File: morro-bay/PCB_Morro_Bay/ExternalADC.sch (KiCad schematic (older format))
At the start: 85 parts, among them SW4 SW_DIP_x12, U10 LM2902, U11 LM2902, U12 LM2902, U14 LM2902, U15 LM2902, U16 LM2902, U17 LM2902, U18 LM2902, U19 LM2902, U20 LM2902, U21 LM2902, U22 LM2902, U23 LM2902, U24 LM2902, U25 LM2902, U26 ADS114S08BIPBSR

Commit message: Even more BOM and footprints
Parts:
- removed C32, C66, C67, C68, C69: 0.1uF, Capacitor_SMD:C_0603_1608Metric_Pad1.05x0.95mm_HandSolder, symbol Device:C
- removed D31, D32, D33, D34: 3.3V, Diode_SMD:D_SOD-323_HandSoldering, symbol Device:D_Zener
- removed R101, R103, R105, R99: 100K, symbol Device:R_US
- removed R106, R107, R108, R109: 500, symbol Device:R_US
- removed U12, U22, U23, U24, U25: LM2902, symbol Amplifier_Operational:LM2902
- added U22: AD620, Package_SO:SOIC-8_3.9x4.9mm_P1.27mm, symbol Amplifier_Instrumentation:AD620
- R74, R76, R78, R80: footprint (none) -> Resistor_SMD:R_0603_1608Metric_Pad1.05x0.95mm_HandSolder; Digikey (none) -> https://www.digikey.ca/product-detail/en/panasonic-electron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; Part Number (none) -> ERJ-PB3B5112V
- R75, R77, R79, R81, R87, R89, R91, R93: footprint (none) -> Resistor_SMD:R_0603_1608Metric_Pad1.05x0.95mm_HandSolder; Digikey (none) -> https://www.digikey.ca/product-detail/en/panasonic-electron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; Part Number (none) -> ERJ-PB3B1003V
- R82, R83, R84, R85, R94, R95, R96, R97: value 500 -> 470; footprint (none) -> Resistor_SMD:R_0603_1608Metric_Pad1.05x0.95mm_HandSolder; Digikey (none) -> https://www.digikey.ca/product-detail/en/stackpole-electron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; Part Number (none) -> RMCF0603FT470R
- R86, R88, R90, R92: footprint (none) -> Resistor_SMD:R_0603_1608Metric_Pad1.05x0.95mm_HandSolder; Digikey (none) -> https://www.digikey.ca/product-detail/en/panasonic-electron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; Part Number (none) -> ERA-3AEB2053V
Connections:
- net 5V_IN_13 is gone; now on net 5V_IN_15: R74.1
- net 5V_IN_14 is gone; now on net 5V_IN_16: R76.1
- net 5V_IN_21 is gone; now on net 5V_IN_15: SW4.1
- net 5V_IN_22 is gone; now on net 5V_IN_16: SW4.2
- net 5V_IN_25 is gone; now on net 10V_IN_7: SW4.5
- net 5V_IN_26 is gone; now on net 10V_IN_8: SW4.6
- net 5V_IN_27 is gone; now on net 10V_IN_9: SW4.7
- net 5V_IN_28 is gone; now on net 10V_IN_9: SW4.8
- net +5V: now also U22.7 (Vs+)
- net 5V_IN_15: no longer R78.1
- net 5V_IN_16: no longer R80.1
- net GND: now also U22.4 (Vs-)
- net 5V_IN_23 renamed 5V_IN_17
- net 5V_IN_17: now also R78.1
- net 5V_IN_24 renamed 5V_IN_18
- net 5V_IN_18: now also R80.1
- net 5V_IN_29: no longer names the net of SW4.9
- net 5V_IN_30: no longer names the net of SW4.10
- net 5V_IN_31: no longer names the net of SW4.11
- net 5V_IN_32: no longer names the net of SW4.12
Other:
- moved on the sheet: C33, C34, C35, R100, R102, R104, R110, R111, R98, SW4, U26

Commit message: BOM BOM BOM BOM baBOM BOM baBOM...
(Imperial march)
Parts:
- removed U14, U18: LM2902, symbol Amplifier_Operational:LM2902
- added unit 1 of U10
- added unit 1 of U11
- U10: renamed from U15; footprint (none) -> Package_SO:SOIC-14_3.9x8.7mm_P1.27mm
- U10: renamed from U16; footprint (none) -> Package_SO:SOIC-14_3.9x8.7mm_P1.27mm
- U10: renamed from U17; footprint (none) -> Package_SO:SOIC-14_3.9x8.7mm_P1.27mm
- U10: renamed from U11; footprint (none) -> Package_SO:SOIC-14_3.9x8.7mm_P1.27mm
- U11: renamed from U19; footprint (none) -> Package_SO:SOIC-14_3.9x8.7mm_P1.27mm
- U11: renamed from U20; footprint (none) -> Package_SO:SOIC-14_3.9x8.7mm_P1.27mm
- U11: renamed from U21; footprint (none) -> Package_SO:SOIC-14_3.9x8.7mm_P1.27mm
- U11: renamed from U10; footprint (none) -> Package_SO:SOIC-14_3.9x8.7mm_P1.27mm
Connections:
- net 10V_IN_9: no longer R92.1
- net 3V3_IN_21: now also U10.3 (+)
- net 3V3_IN_22: now also U10.5 (+); no longer U10.3 (+)
- net 3V3_IN_23: now also U10.10 (+); no longer U10.3 (+)
- net 3V3_IN_24: now also U10.12 (+); no longer U10.3 (+)
- net 3V3_IN_25: now also U11.3 (+)
- net 3V3_IN_26: now also U11.5 (+); no longer U11.3 (+)
- net 3V3_IN_27: now also U11.10 (+); no longer U11.3 (+)
- net 3V3_IN_28: now also U11.12 (+); no longer U11.3 (+)
- net IN_21_BUFFERED: now also U10.1, U10.2 (-)
- net IN_22_BUFFERED: now also U10.6 (-), U10.7; no longer U10.1, U10.2 (-)
- net IN_23_BUFFERED: now also U10.8, U10.9 (-); no longer U10.1, U10.2 (-)
- net IN_24_BUFFERED: now also U10.13 (-), U10.14; no longer U10.1, U10.2 (-)
- net IN_25_BUFFERED: now also U11.1, U11.2 (-)
- net IN_26_BUFFERED: now also U11.6 (-), U11.7; no longer U11.1, U11.2 (-)
- net IN_27_BUFFERED: now also U11.8, U11.9 (-); no longer U11.1, U11.2 (-)
- net IN_28_BUFFERED: now also U11.13 (-), U11.14; no longer U11.1, U11.2 (-)
- new net 10V_IN_10: R92.1
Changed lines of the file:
@@
 Wire Wire Line
 	850  1100 850  1150
-$Comp
-L Amplifier_Operational:LM2902 U?
-U 1 1 5E5F6D49
-P 1500 1250
-AR Path="/5E5F6D49" Ref="U?"  Part="1"
-AR Path="/5E59A680/5E5F6D49" Ref="U?"  Part="1"
-AR Path="/5E828D93/5E5F6D49" Ref="U?"  Part="1"
-AR Path="/5E59A680/5E5467E7/5E5F6D49" Ref="U14"  Part="1"
-F 0 "U14" H 1500 1617 50  0000 C CNN
-F 1 "LM2902" H 1500 1526 50  0000 C CNN
-F 2 "" H 1450 1350 50  0001 C CNN
-F 3 "http://www.ti.com/lit/ds/symlink/lm2902-n.pdf" H 1550 1450 50  0001 C CNN
-	1    1500 1250
-	1    0    0    -1
-$EndComp
 Wire Wire Line
 	850  1150 1200 1150
@@
 $Comp
 L Amplifier_Operational:LM2902 U?
-U 1 1 5E5F6D89
+U 2 1 5E5F6D89
 P 1500 2450
 AR Path="/5E5F6D89" Ref="U?"  Part="1"
 AR Path="/5E59A680/5E5F6D89" Ref="U?"  Part="1"
 AR Path="/5E828D93/5E5F6D89" Ref="U?"  Part="1"
-AR Path="/5E59A680/5E5467E7/5E5F6D89" Ref="U15"  Part="1"
-F 0 "U15" H 1500 2817 50  0000 C CNN
+AR Path="/5E59A680/5E5467E7/5E5F6D89" Ref="U10"  Part="2"
+F 0 "U10" H 1500 2817 50  0000 C CNN
 F 1 "LM2902" H 1500 2726 50  0000 C CNN
-F 2 "" H 1450 2550 50  0001 C CNN
+F 2 "Package_SO:SOIC-14_3.9x8.7mm_P1.27mm" H 1450 2550 50  0001 C CNN
 F 3 "http://www.ti.com/lit/ds/symlink/lm2902-n.pdf" H 1550 2650 50  0001 C CNN
-	1    1500 2450
+	2    1500 2450
 	1    0    0    -1
 $EndComp
@@
 $Comp
 L Amplifier_Operational:LM2902 U?
-U 1 1 5E5F6DC9
+U 3 1 5E5F6DC9
 P 1500 3650
 AR Path="/5E5F6DC9" Ref="U?"  Part="1"
 AR Path="/5E59A680/5E5F6DC9" Ref="U?"  Part="1"
 AR Path="/5E828D93/5E5F6DC9" Ref="U?"  Part="1"
-AR Path="/5E59A680/5E5467E7/5E5F6DC9" Ref="U16"  Part="1"
-F 0 "U16" H 1500 4017 50  0000 C CNN
+AR Path="/5E59A680/5E5467E7/5E5F6DC9" Ref="U10"  Part="3"
+F 0 "U10" H 1500 4017 50  0000 C CNN
 F 1 "LM2902" H 1500 3926 50  0000 C CNN
-F 2 "" H 1450 3750 50  0001 C CNN
+F 2 "Package_SO:SOIC-14_3.9x8.7mm_P1.27mm" H 1450 3750 50  0001 C CNN
 F 3 "http://www.ti.com/lit/ds/symlink/lm2902-n.pdf" H 1550 3850 50  0001 C CNN
-	1    1500 3650
+	3    1500 3650
 	1    0    0    -1
 $EndComp
@@
 $Comp
 L Amplifier_Operational:LM2902 U?
-U 1 1 5E5F6E09
+U 4 1 5E5F6E09
 P 1500 4800
 AR Path="/5E5F6E09" Ref="U?"  Part="1"
 AR Path="/5E59A680/5E5F6E09" Ref="U?"  Part="1"
 AR Path="/5E828D93/5E5F6E09" Ref="U?"  Part="1"
-AR Path="/5E59A680/5E5467E7/5E5F6E09" Ref="U17"  Part="1"
-F 0 "U17" H 1500 5167 50  0000 C CNN
+AR Path="/5E59A680/5E5467E7/5E5F6E09" Ref="U10"  Part="4"
+F 0 "U10" H 1500 5167 50  0000 C CNN
 F 1 "LM2902" H 1500 5076 50  0000 C CNN
-F 2 "" H 1450 4900 50  0001 C CNN
+F 2 "Package_SO:SOIC-14_3.9x8.7mm_P1.27mm" H 1450 4900 50  0001 C CNN
 F 3 "http://www.ti.com/lit/ds/symlink/lm2902-n.pdf" H 1550 5000 50  0001 C CNN
-	1    1500 4800
+	4    1500 4800
 	1    0    0    -1
 $EndComp
@@
 AR Path="/5E59A680/5E5F6E3A" Ref="U?"  Part="5"
 AR Path="/5E828D93/5E5F6E3A" Ref="U?"  Part="5"
-AR Path="/5E59A680/5E5467E7/5E5F6E3A" Ref="U11"  Part="5"
-F 0 "U11" H 1700 5850 50  0000 C CNN
+AR Path="/5E59A680/5E5467E7/5E5F6E3A" Ref="U10"  Part="5"
+F 0 "U10" H 1700 5850 50  0000 C CNN
 F 1 "LM2902" H 1700 5750 50  0000 C CNN
-F 2 "" H 1550 5900 50  0001 C CNN
+F 2 "Package_SO:SOIC-14_3.9x8.7mm_P1.27mm" H 1550 5900 50  0001 C CNN
 F 3 "http://www.ti.com/lit/ds/symlink/lm2902-n.pdf" H 1650 6000 50  0001 C CNN
 	5    1600 5800
@@
 Wire Wire Line
 	3050 1100 3050 1150
-$Comp
-L Amplifier_Operational:LM2902 U?
-U 1 1 5E6049B1
-P 3700 1250
-AR Path="/5E6049B1" Ref="U?"  Part="1"
-AR Path="/5E59A680/5E6049B1" Ref="U?"  Part="1"
-AR Path="/5E828D93/5E6049B1" Ref="U?"  Part="1"
-AR Path="/5E59A680/5E5467E7/5E6049B1" Ref="U18"  Part="1"
-F 0 "U18" H 3700 1617 50  0000 C CNN
-F 1 "LM2902" H 3700 1526 50  0000 C CNN
-F 2 "" H 3650 1350 50  0001 C CNN
-F 3 "http://www.ti.com/lit/ds/symlink/lm2902-n.pdf" H 3750 1450 50  0001 C CNN
-	1    3700 1250
-	1    0    0    -1
-$EndComp
 Wire Wire Line
 	3050 1150 3400 1150
@@
 $Comp
 L Amplifier_Operational:LM2902 U?
-U 1 1 5E604A0D
+U 2 1 5E604A0D
 P 3700 2450
 AR Path="/5E604A0D" Ref="U?"  Part="1"
 AR Path="/5E59A680/5E604A0D" Ref="U?"  Part="1"
 AR Path="/5E828D93/5E604A0D" Ref="U?"  Part="1"
-AR Path="/5E59A680/5E5467E7/5E604A0D" Ref="U19"  Part="1"
-F 0 "U19" H 3700 2817 50  0000 C CNN
+AR Path="/5E59A680/5E5467E7/5E604A0D" Ref="U11"  Part="2"
+F 0 "U11" H 3700 2817 50  0000 C CNN
 F 1 "LM2902" H 3700 2726 50  0000 C CNN
-F 2 "" H 3650 2550 50  0001 C CNN
+F 2 "Package_SO:SOIC-14_3.9x8.7mm_P1.27mm" H 3650 2550 50  0001 C CNN
 F 3 "http://www.ti.com/lit/ds/symlink/lm2902-n.pdf" H 3750 2650 50  0001 C CNN
-	1    3700 2450
+	2    3700 2450
 	1    0    0    -1
 $EndComp
@@
 $Comp
 L Amplifier_Operational:LM2902 U?
-U 1 1 5E604A69
+U 3 1 5E604A69
 P 3700 3650
 AR Path="/5E604A69" Ref="U?"  Part="1"
 AR Path="/5E59A680/5E604A69" Ref="U?"  Part="1"
 AR Path="/5E828D93/5E604A69" Ref="U?"  Part="1"
-AR Path="/5E59A680/5E5467E7/5E604A69" Ref="U20"  Part="1"
-F 0 "U20" H 3700 4017 50  0000 C CNN
+AR Path="/5E59A680/5E5467E7/5E604A69" Ref="U11"  Part="3"
+F 0 "U11" H 3700 4017 50  0000 C CNN
 F 1 "LM2902" H 3700 3926 50  0000 C CNN
-F 2 "" H 3650 3750 50  0001 C CNN
+F 2 "Package_SO:SOIC-14_3.9x8.7mm_P1.27mm" H 3650 3750 50  0001 C CNN
 F 3 "http://www.ti.com/lit/ds/symlink/lm2902-n.pdf" H 3750 3850 50  0001 C CNN
-	1    3700 3650
+	3    3700 3650
 	1    0    0    -1
 $EndComp
@@
 $Comp
 L Amplifier_Operational:LM2902 U?
-U 1 1 5E604AC5
+U 4 1 5E604AC5
 P 3700 4800
 AR Path="/5E604AC5" Ref="U?"  Part="1"
 AR Path="/5E59A680/5E604AC5" Ref="U?"  Part="1"
 AR Path="/5E828D93/5E604AC5" Ref="U?"  Part="1"
-AR Path="/5E59A680/5E5467E7/5E604AC5" Ref="U21"  Part="1"
-F 0 "U21" H 3700 5167 50  0000 C CNN
+AR Path="/5E59A680/5E5467E7/5E604AC5" Ref="U11"  Part="4"
+F 0 "U11" H 3700 5167 50  0000 C CNN
 F 1 "LM2902" H 3700 5076 50  0000 C CNN
-F 2 "" H 3650 4900 50  0001 C CNN
+F 2 "Package_SO:SOIC-14_3.9x8.7mm_P1.27mm" H 3650 4900 50  0001 C CNN
 F 3 "http://www.ti.com/lit/ds/symlink/lm2902-n.pdf" H 3750 5000 50  0001 C CNN
-	1    3700 4800
+	4    3700 4800
 	1    0    0    -1
 $EndComp
@@
 AR Path="/5E59A680/5E604B0A" Ref="U?"  Part="5"
 AR Path="/5E828D93/5E604B0A" Ref="U?"  Part="5"
-AR Path="/5E59A680/5E5467E7/5E604B0A" Ref="U10"  Part="5"
-F 0 "U10" H 3900 5850 50  0000 C CNN
+AR Path="/5E59A680/5E5467E7/5E604B0A" Ref="U11"  Part="5"
+F 0 "U11" H 3900 5850 50  0000 C CNN
 F 1 "LM2902" H 3900 5750 50  0000 C CNN
-F 2 "" H 3750 5900 50  0001 C CNN
+F 2 "Package_SO:SOIC-14_3.9x8.7mm_P1.27mm" H 3750 5900 50  0001 C CNN
 F 3 "http://www.ti.com/lit/ds/symlink/lm2902-n.pdf" H 3850 6000 50  0001 C CNN
 	5    3800 5800
@@
 10V_IN_9
 Text GLabel 3100 4300 2    50   Input ~ 0
-10V_IN_9
+10V_IN_10
 $Comp
 L Device:C C?
@@
 Connection ~ 4400 4800
 Connection ~ 2200 4800
+$Comp
+L Amplifier_Operational:LM2902 U?
+U 1 1 5E894B14
+P 1500 1250
+AR Path="/5E894B14" Ref="U?"  Part="1"
+AR Path="/5E59A680/5E894B14" Ref="U?"  Part="1"
+AR Path="/5E828D93/5E894B14" Ref="U?"  Part="1"
+AR Path="/5E59A680/5E5467E7/5E894B14" Ref="U10"  Part="1"
+F 0 "U10" H 1500 1617 50  0000 C CNN
+F 1 "LM2902" H 1500 1526 50  0000 C CNN
+F 2 "Package_SO:SOIC-14_3.9x8.7mm_P1.27mm" H 1450 1350 50  0001 C CNN
+F 3 "http://www.ti.com/lit/ds/symlink/lm2902-n.pdf" H 1550 1450 50  0001 C CNN
+F 4 "https://www.digikey.ca/product-detail/en/texas-instruments/LM2902LVIDR/296-51255-1-ND/9745619" H 1500 1250 50  0001 C CNN "Digikey"
+F 5 "LM2902LVIDR" H 1500 1250 50  0001 C CNN "Part Number"
+	1    1500 1250
+	1    0    0    -1
+$EndComp
+$Comp
+L Amplifier_Operational:LM2902 U?
+U 1 1 5E8A38F1
+P 3700 1250
+AR Path="/5E8A38F1" Ref="U?"  Part="1"
+AR Path="/5E59A680/5E8A38F1" Ref="U?"  Part="1"
+AR Path="/5E828D93/5E8A38F1" Ref="U?"  Part="1"
+AR Path="/5E59A680/5E5467E7/5E8A38F1" Ref="U11"  Part="1"
+F 0 "U11" H 3700 1617 50  0000 C CNN
+F 1 "LM2902" H 3700 1526 50  0000 C CNN
+F 2 "Package_SO:SOIC-14_3.9x8.7mm_P1.27mm" H 3650 1350 50  0001 C CNN
+F 3 "http://www.ti.com/lit/ds/symlink/lm2902-n.pdf" H 3750 1450 50  0001 C CNN
+F 4 "https://www.digikey.ca/product-detail/en/texas-instruments/LM2902LVIDR/296-51255-1-ND/9745619" H 3700 1250 50  0001 C CNN "Digikey"
+F 5 "LM2902LVIDR" H 3700 1250 50  0001 C CNN "Part Number"
+	1    3700 1250
+	1    0    0    -1
+$EndComp
 $EndSCHEMATC

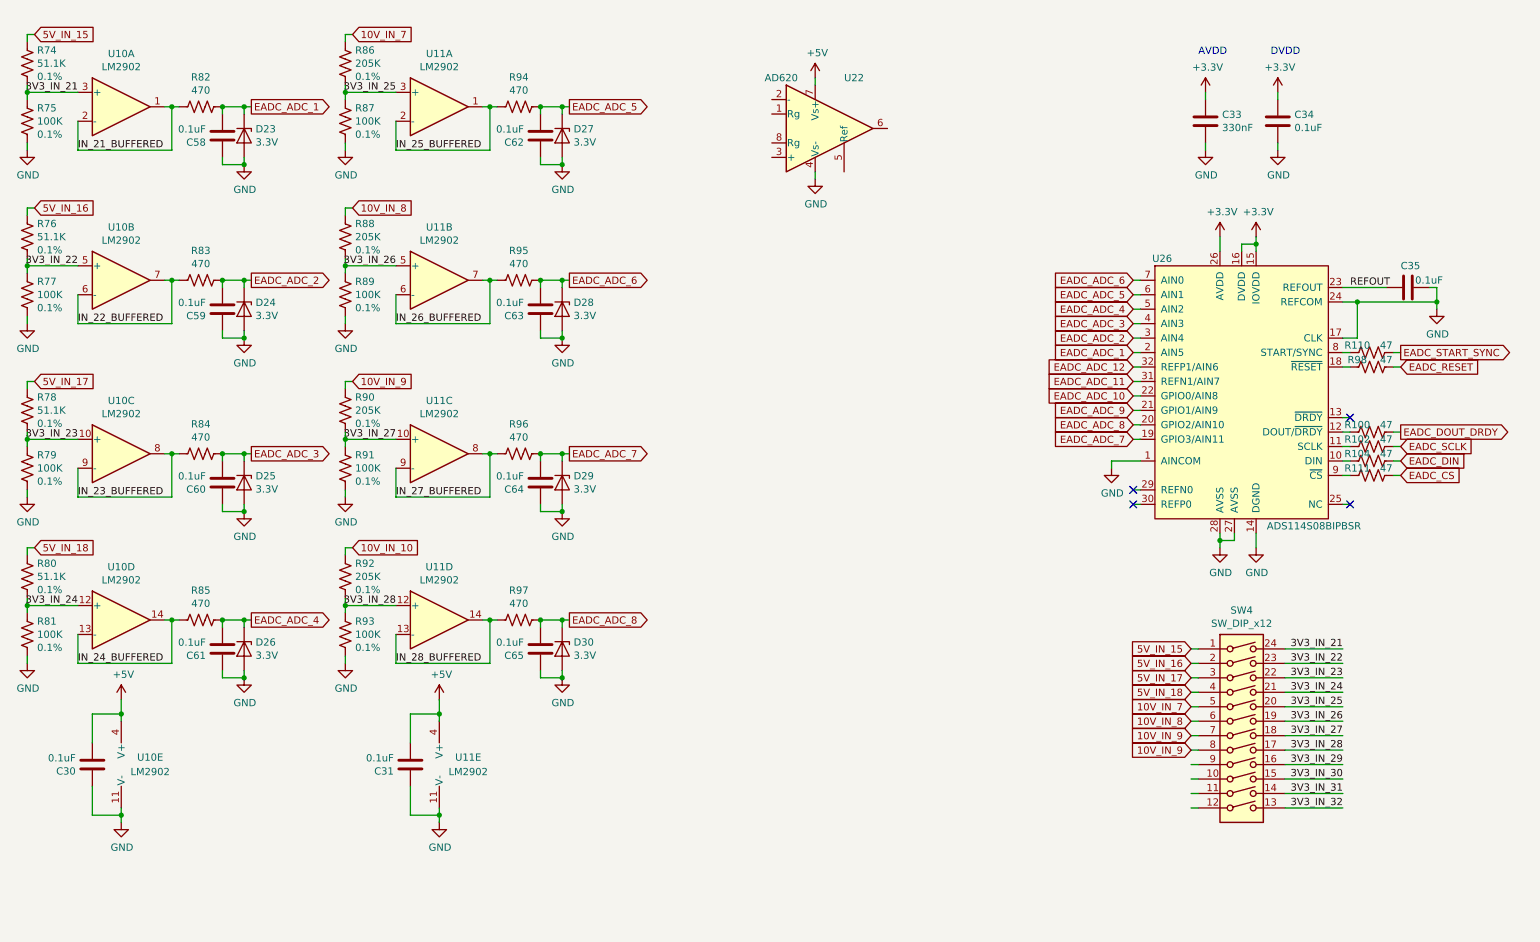
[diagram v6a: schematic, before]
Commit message: Start layout, finish BOM
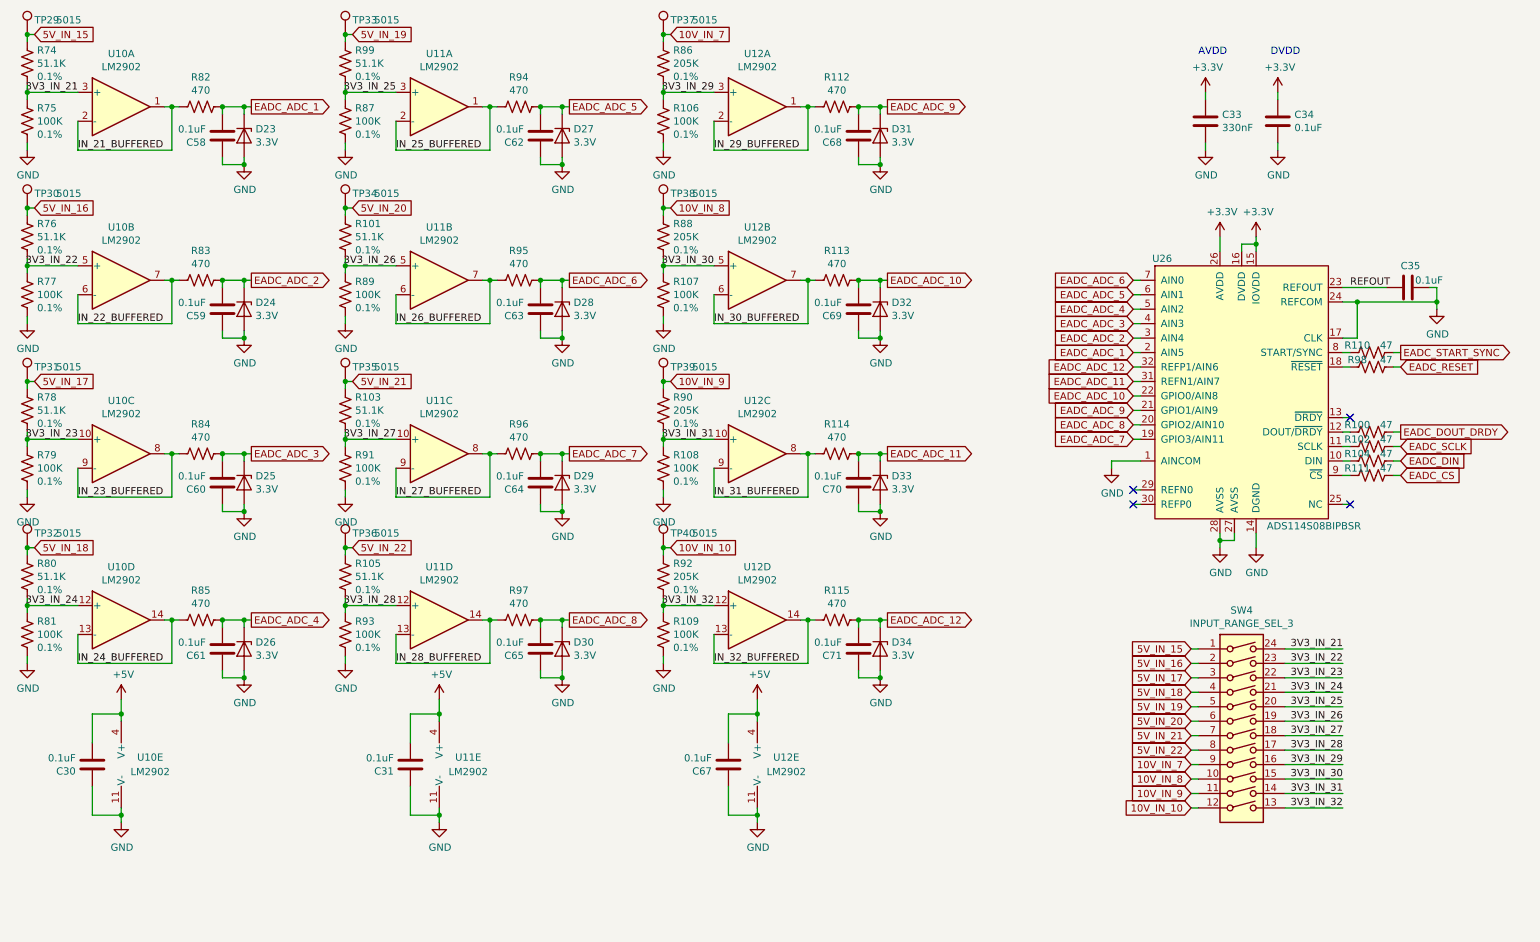
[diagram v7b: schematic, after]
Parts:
- removed U22: AD620, Package_SO:SOIC-8_3.9x4.9mm_P1.27mm, symbol Amplifier_Instrumentation:AD620
- added C67, C68, C69, C70, C71: 0.1uF, Capacitor_SMD:C_0603_1608Metric_Pad1.05x0.95mm_HandSolder, symbol Device:C
- added D31, D32, D33, D34: 3.3V, Diode_SMD:D_SOD-323_HandSoldering, symbol Device:D_Zener
- added R101, R103, R105, R99: 51.1K, Resistor_SMD:R_0603_1608Metric_Pad1.05x0.95mm_HandSolder, symbol Device:R_US
- added R106, R107, R108, R109: 100K, Resistor_SMD:R_0603_1608Metric_Pad1.05x0.95mm_HandSolder, symbol Device:R_US
- added R112, R113, R114, R115: 470, Resistor_SMD:R_0603_1608Metric_Pad1.05x0.95mm_HandSolder, symbol Device:R_US
- added TP29, TP30, TP31, TP32, TP33, TP34, TP35, TP36, TP37, TP38, TP39, TP40: 5015, TestPoint:TestPoint_Keystone_5015_Micro-Minature, symbol Connector:TestPoint
- added U12: LM2902, Package_SO:SOIC-14_3.9x8.7mm_P1.27mm, symbol Amplifier_Operational:LM2902
- SW4: value SW_DIP_x12 -> INPUT_RANGE_SEL_3; footprint (none) -> Button_Switch_SMD:SW_DIP_SPSTx12_Slide_6.7x32.04mm_W8.61mm_P2.54mm_LowProfile; Digikey (none) -> https://www.digikey.ca/product-detail/en/cui-devices/DS04-2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; Part Number (none) -> DS04-254-2-12BK-SMT
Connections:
- net +5V: now also C67.2, U12.4 (V+)
- net 10V_IN_10: now also SW4.12, TP40.1
- net 10V_IN_7: now also SW4.9, TP37.1; no longer SW4.5
- net 10V_IN_8: now also SW4.10, TP38.1; no longer SW4.6
- net 10V_IN_9: now also SW4.11, TP39.1; no longer SW4.7, SW4.8
- net 3V3_IN_25: now also R99.2; no longer R86.2
- net 3V3_IN_26: now also R101.2; no longer R88.2
- net 3V3_IN_27: now also R103.2; no longer R90.2
- net 3V3_IN_28: now also R105.2; no longer R92.2
- net 3V3_IN_29: now also R86.2, R106.1, U12.3 (+)
- net 3V3_IN_30: now also R88.2, R107.1, U12.5 (+)
- net 3V3_IN_31: now also R90.2, R108.1, U12.10 (+)
- net 3V3_IN_32: now also R92.2, R109.1, U12.12 (+)
- net 5V_IN_15: now also TP29.1
- net 5V_IN_16: now also TP30.1
- net 5V_IN_17: now also TP31.1
- net 5V_IN_18: now also TP32.1
- net EADC_ADC_10: now also C69.2, D32.1 (K), R113.1
- net EADC_ADC_11: now also C70.2, D33.1 (K), R114.1
- net EADC_ADC_12: now also C71.2, D34.1 (K), R115.1
- net EADC_ADC_9: now also C68.2, D31.1 (K), R112.1
- net GND: now also C67.1, C68.1, C69.1, C70.1, C71.1, D31.2 (A), D32.2 (A), D33.2 (A), D34.2 (A), R106.2, R107.2, R108.2, R109.2, U12.11 (V-)
- new net 5V_IN_19: R99.1, SW4.5, TP33.1
- new net 5V_IN_20: R101.1, SW4.6, TP34.1
- new net 5V_IN_21: R103.1, SW4.7, TP35.1
- new net 5V_IN_22: R105.1, SW4.8, TP36.1
- new net IN_29_BUFFERED: R112.2, U12.1, U12.2 (-)
- new net IN_30_BUFFERED: R113.2, U12.6 (-), U12.7
- new net IN_31_BUFFERED: R114.2, U12.8, U12.9 (-)
- new net IN_32_BUFFERED: R115.2, U12.13 (-), U12.14
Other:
- moved on the sheet: R86, R88, R90, R92
